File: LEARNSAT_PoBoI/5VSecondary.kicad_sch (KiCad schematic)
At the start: 17 parts, among them Q6 SI7164DP-T1-GE3, Q8 SI5418DU-T1-GE3, U19 INA219AIDCNR, U24 LTC4231IUD-2#TRPBF

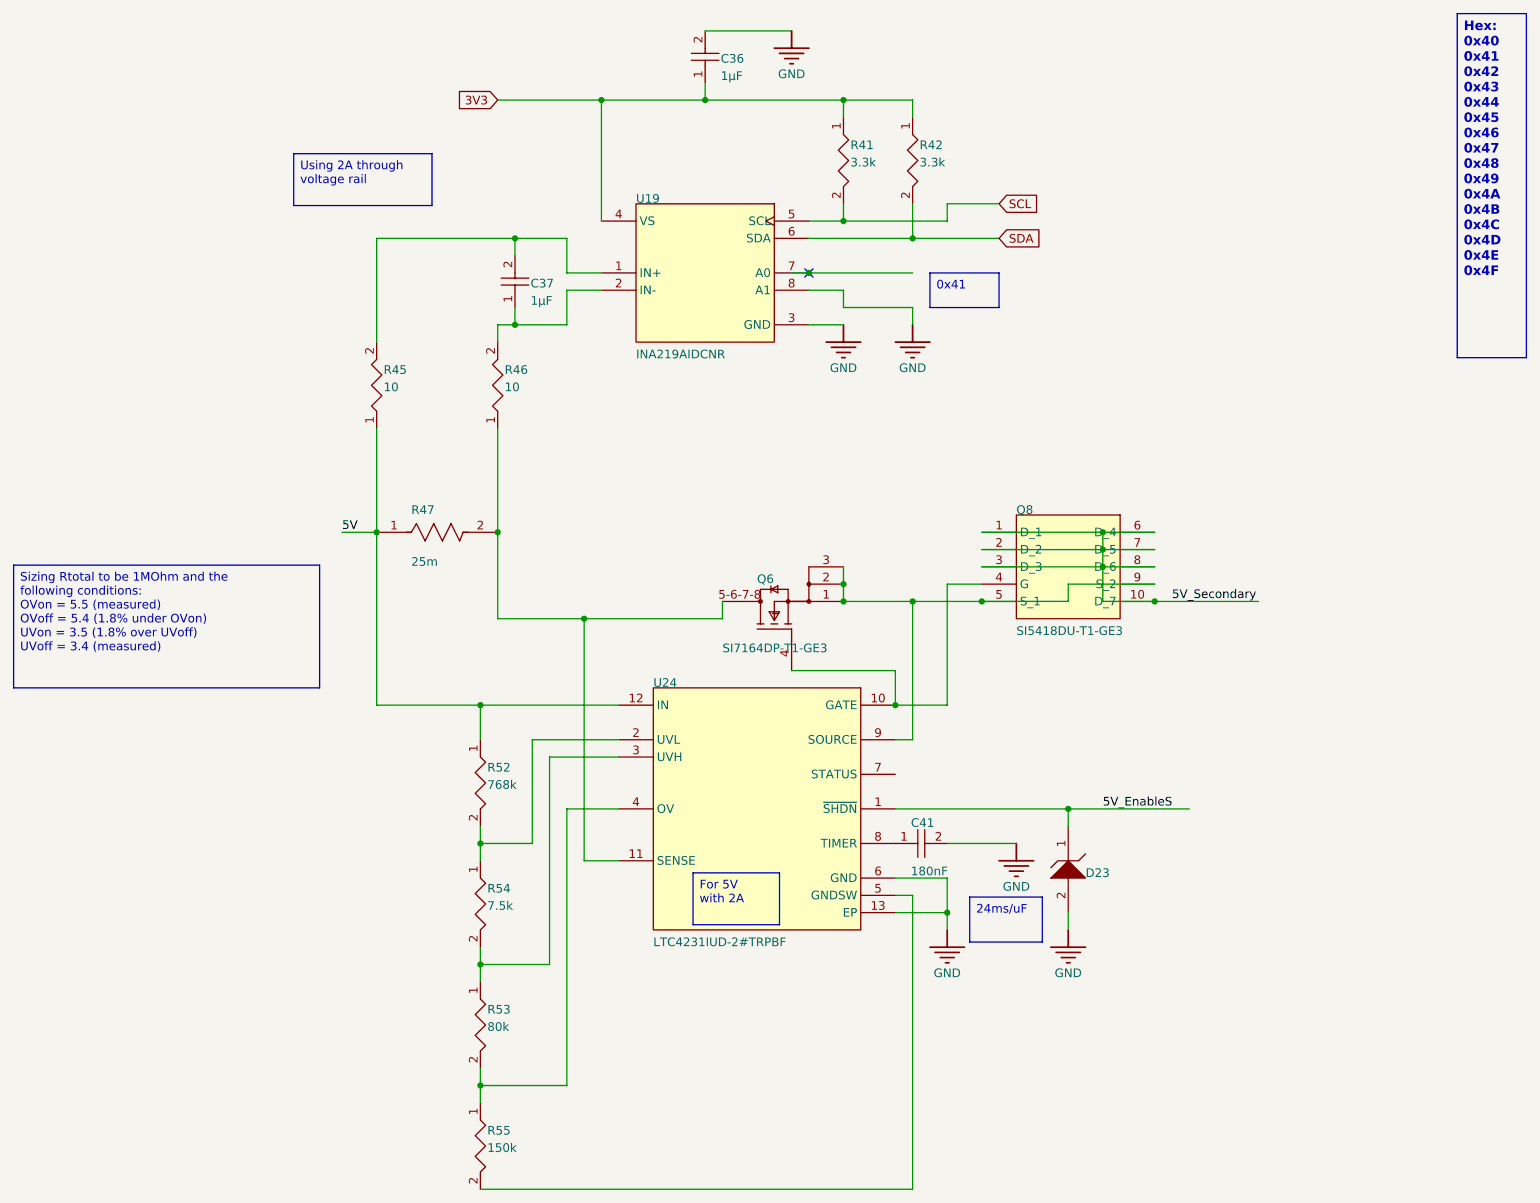
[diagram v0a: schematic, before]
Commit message: Added footprints
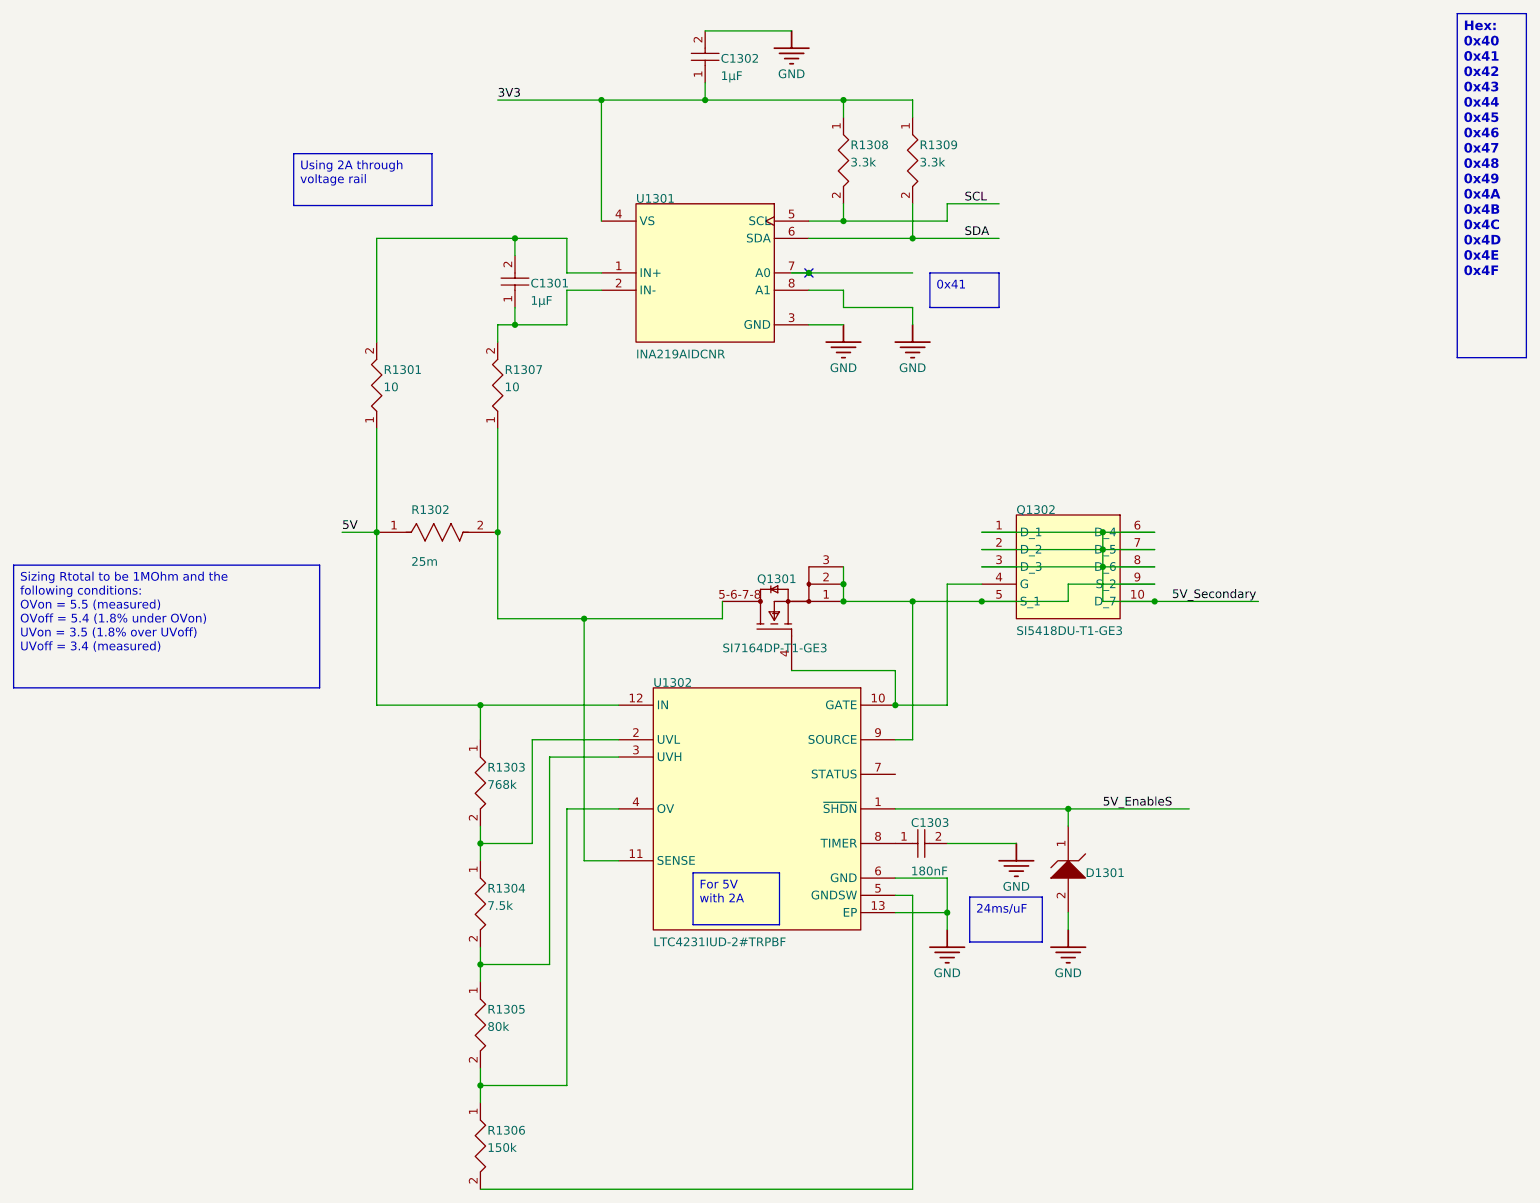
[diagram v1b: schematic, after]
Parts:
- C1301: renamed from C37; footprint CAPC1608X90X40LL10T20 -> Capacitor_SMD:C_0603_1608Metric
- C1302: renamed from C36; footprint CAPC1608X90X35ML15T15 -> Capacitor_SMD:C_0603_1608Metric
- C1303: renamed from C41; footprint FP-C0805C-DN-IPC_A -> Capacitor_SMD:C_0805_2012Metric
- D1301: renamed from D23; footprint ONSC-SOD-323-2-477-02_V -> Diode_SMD:D_SOD-323
- Q1301: renamed from Q6; footprint Vishay_S17-0173-SINGLE_MFG -> Package_SO:Vishay_PowerPAK_1212-8_Single
- Q1302: renamed from Q8; footprint SI5418DU-T1-GE3-Footprint-1 -> Package_SO:Vishay_PowerPAK_1212-8_Single
- R1301: renamed from R45; footprint RESC0402(1005)_L -> Resistor_SMD:R_0402_1005Metric
- R1302: renamed from R47; footprint FP-CSR1206-IPC_C -> Resistor_SMD:R_1206_3216Metric
- R1303: renamed from R52; footprint RESC0402(1005)_L -> Resistor_SMD:R_0402_1005Metric
- R1304: renamed from R54; footprint FP-CRCW1206-e3-IPC_A -> Resistor_SMD:R_1206_3216Metric
- R1305: renamed from R53; footprint FP-PTN0603-IPC_B -> Resistor_SMD:R_0603_1608Metric
- R1306: renamed from R55; footprint FP-RT1206-IPC_C -> Resistor_SMD:R_1206_3216Metric
- R1307: renamed from R46; footprint RESC0402(1005)_L -> Resistor_SMD:R_0402_1005Metric
- R1308: renamed from R41; footprint FP-CRCW1210-e3-IPC_C -> Resistor_SMD:R_1210_3225Metric
- R1309: renamed from R42; footprint FP-CRCW1210-e3-IPC_C -> Resistor_SMD:R_1210_3225Metric
- U1301: renamed from U19; footprint FP-DCN0008A-IPC_A -> INA219AIDCNR:SOT65P280X145-8N
- U1302: renamed from U24; footprint FP-UD-12-05-08-1855-IPC_A -> LTC4231IUD-2_TRPBF:QFN50P300X300X80-13N

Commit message: Add files via upload
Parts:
- C36: renamed from C1302; footprint Capacitor_SMD:C_0603_1608Metric -> CAPC1608X90X35ML15T15
- C37: renamed from C1301; footprint Capacitor_SMD:C_0603_1608Metric -> CAPC1608X90X40LL10T20
- C41: renamed from C1303; footprint Capacitor_SMD:C_0805_2012Metric -> FP-C0805C-DN-IPC_A
- D23: renamed from D1301; footprint Diode_SMD:D_SOD-323 -> ONSC-SOD-323-2-477-02_V
- Q6: renamed from Q1301; footprint Package_SO:Vishay_PowerPAK_1212-8_Single -> Vishay_S17-0173-SINGLE_MFG
- Q8: renamed from Q1302; footprint Package_SO:Vishay_PowerPAK_1212-8_Single -> SI5418DU-T1-GE3-Footprint-1
- R41: renamed from R1308; footprint Resistor_SMD:R_1210_3225Metric -> FP-CRCW1210-e3-IPC_C
- R42: renamed from R1309; footprint Resistor_SMD:R_1210_3225Metric -> FP-CRCW1210-e3-IPC_C
- R45: renamed from R1301; footprint Resistor_SMD:R_0402_1005Metric -> RESC0402(1005)_L
- R46: renamed from R1307; footprint Resistor_SMD:R_0402_1005Metric -> RESC0402(1005)_L
- R47: renamed from R1302; footprint Resistor_SMD:R_1206_3216Metric -> FP-CSR1206-IPC_C
- R52: renamed from R1303; footprint Resistor_SMD:R_0402_1005Metric -> RESC0402(1005)_L
- R53: renamed from R1305; footprint Resistor_SMD:R_0603_1608Metric -> FP-PTN0603-IPC_B
- R54: renamed from R1304; footprint Resistor_SMD:R_1206_3216Metric -> FP-CRCW1206-e3-IPC_A
- R55: renamed from R1306; footprint Resistor_SMD:R_1206_3216Metric -> FP-RT1206-IPC_C
- U19: renamed from U1301; footprint INA219AIDCNR:SOT65P280X145-8N -> FP-DCN0008A-IPC_A
- U24: renamed from U1302; footprint LTC4231IUD-2_TRPBF:QFN50P300X300X80-13N -> FP-UD-12-05-08-1855-IPC_A
